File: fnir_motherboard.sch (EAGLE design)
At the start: 44 parts, among them IC1 LTC2494, IC3 AD712R, U2 ATMEGA8U2QFN, X2 USB-SMD-NS, Y1 16MHz

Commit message: new version desinged
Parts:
- added R16: 200, adafruit:R-US_R1206
- added TP1: PTR1B1,27, testpad:PTR1B1,27
- C1, C2, C3, C4, C5, C6, C7, C8: device adafruit:C-USC0805 -> adafruit:C-USC1206
- C10, C9: value (none) -> 0.1uF; device adafruit:C-USC0805 -> adafruit:C-USC1206
- R1: value (none) -> 200; device adafruit:R-US_R0805 -> adafruit:R-US_R1206
- R10, R11, R12, R13, R14, R15, R28, R29, R5, R6, R7, R8, R9: device adafruit:R-US_R0805 -> adafruit:R-US_R1206
- R2: value (none) -> 10k
- R3, R4: value (none) -> 30k; device adafruit:R-US_R0805 -> adafruit:R-US_R1206
- U2: value ATMEGA8U2QFN -> ATMEGA8U2AU; device sparkfun:ATMEGA8U2QFN -> sparkfun:ATMEGA8U2AU
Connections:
- new net N$23: R16.2, SV1.2
- net +5V: now also R2.A; no longer R2.E
- net AGND: now also R2.E; no longer R2.A
- net GND: now also R16.1; no longer SV1.2
- net IR8: now also IC1.CH9; no longer IC1.CH8
- net IR9: now also IC1.CH11; no longer IC1.CH9
- net N$1: now also Q2.G; no longer Q6.G
- net N$12: now also TP1.TP
- net N$2: now also Q1.G; no longer Q7.G
- net N$3: now also Q9.G, U2.PD5; no longer Q5.G, U2.PD4
- net N$4: now also Q4.G; no longer Q1.G
- net N$5: now also Q5.G; no longer Q4.G
- net N$6: now also Q7.G; no longer Q9.G
- net N$7: now also Q6.G; no longer Q2.G
- net N$8: now also U2.PD4; no longer U2.PD5
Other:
- moved on the sheet: C1, C10, C15, C2, C3, C4, C5, C6, C7, C8, C9, IC1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

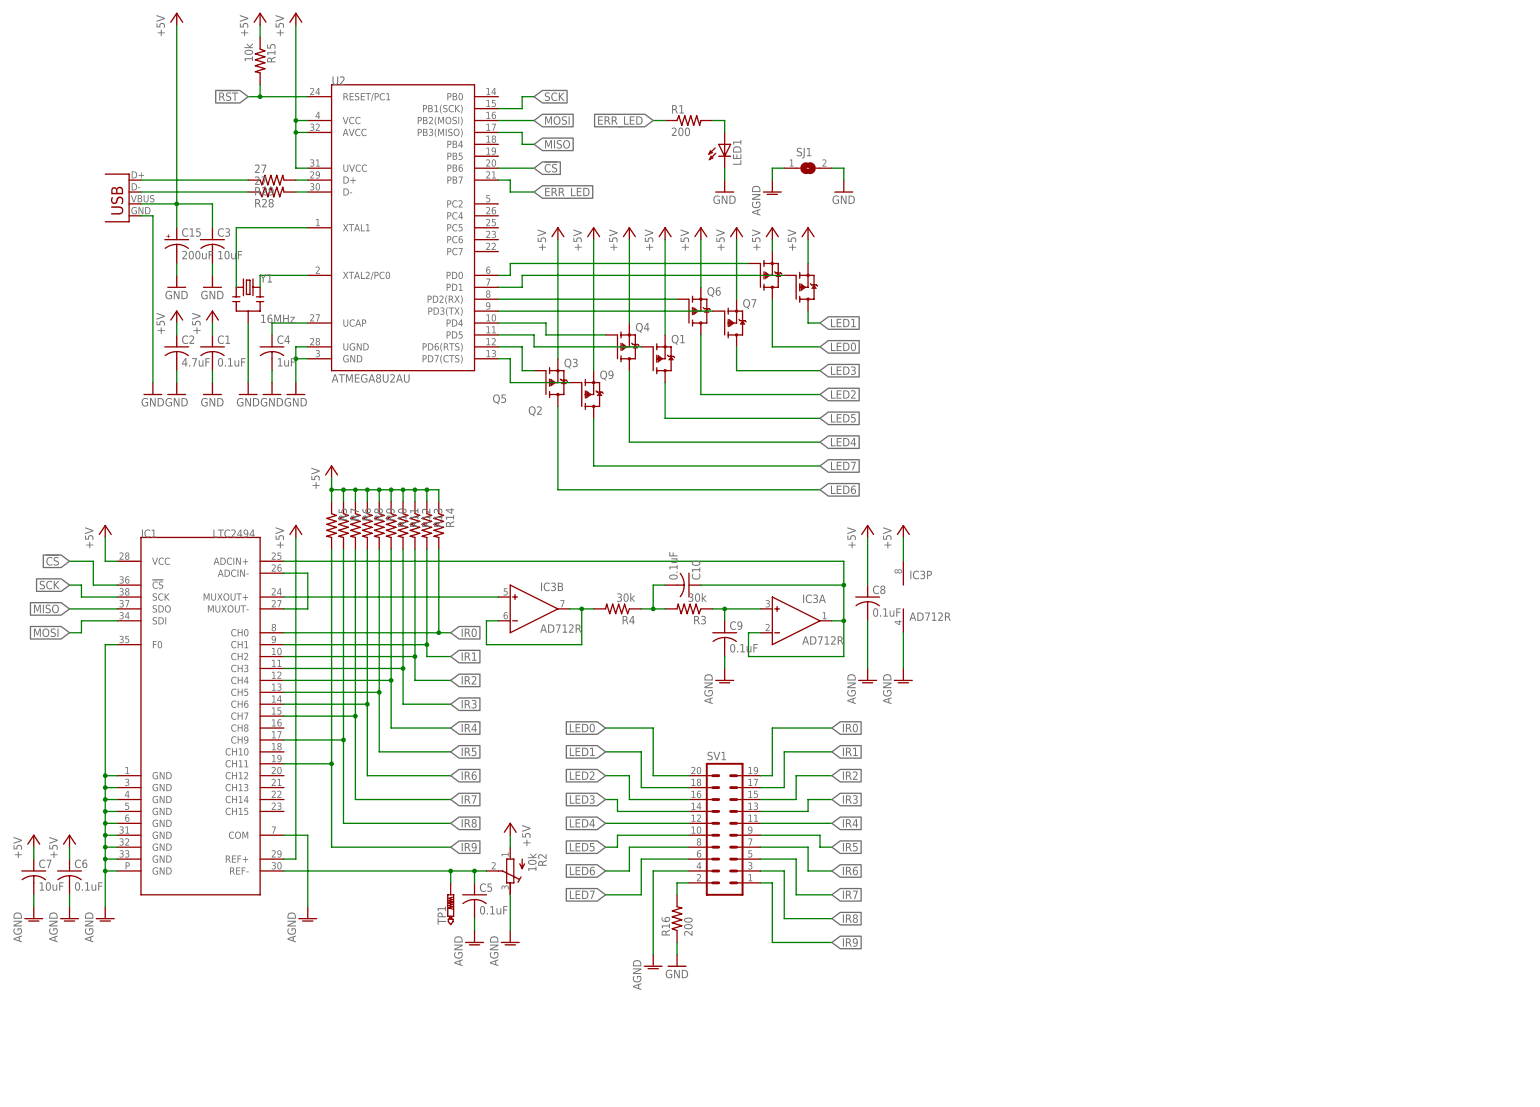
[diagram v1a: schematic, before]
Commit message: slight changes to pour layouts for ground and agnd (merged)
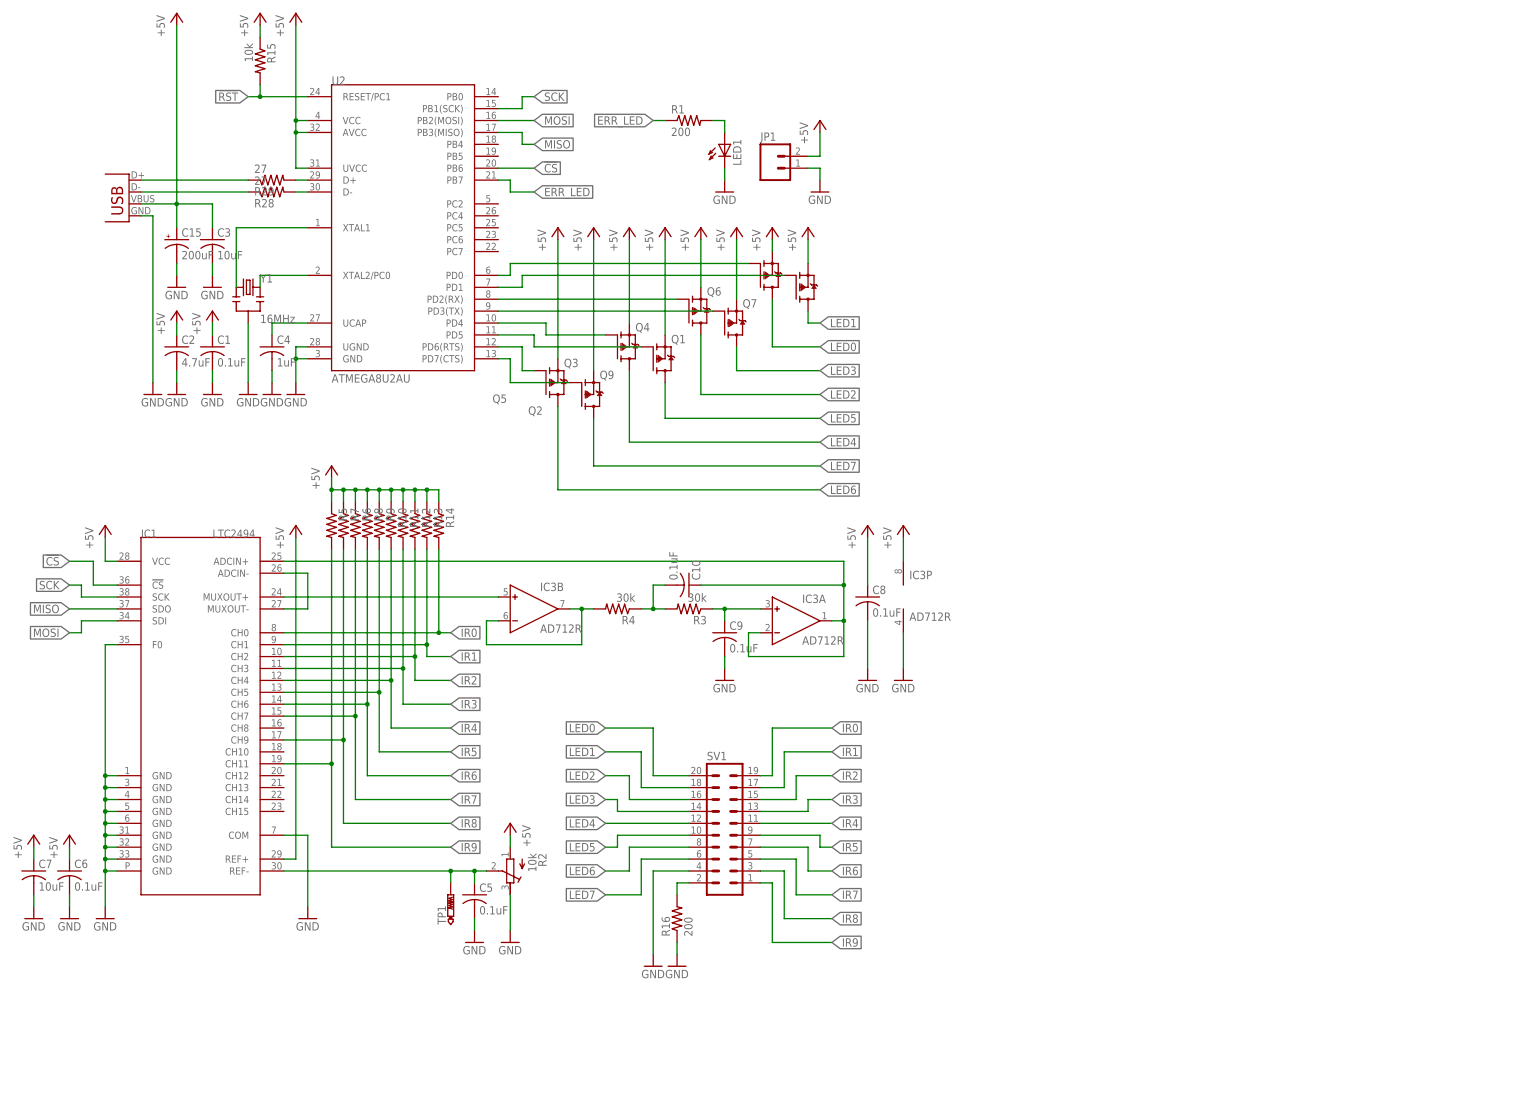
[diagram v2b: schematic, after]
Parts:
- removed SJ1: (no value), jumper:SJ
- added JP1: (no value), sparkfun:M02PTH
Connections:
- removed net AGND: C5.2, C6.2, C7.2, C8.2, C9.2, IC1.COM, IC1.F0, IC1.GND@0, IC1.GND@1, IC1.GND@2, IC1.GND@3, IC1.GND@4, IC1.GND@5, IC1.GND@6, IC1.GND@7, IC1.GND@8, IC3P.V-, R2.E, SJ1.1, SV1.4
- net +5V: now also JP1.2
- net GND: now also C5.2, C6.2, C7.2, C8.2, C9.2, IC1.COM, IC1.F0, IC1.GND@0, IC1.GND@1, IC1.GND@2, IC1.GND@3, IC1.GND@4, IC1.GND@5, IC1.GND@6, IC1.GND@7, IC1.GND@8, IC3P.V-, JP1.1, R2.E, SV1.4; no longer SJ1.2

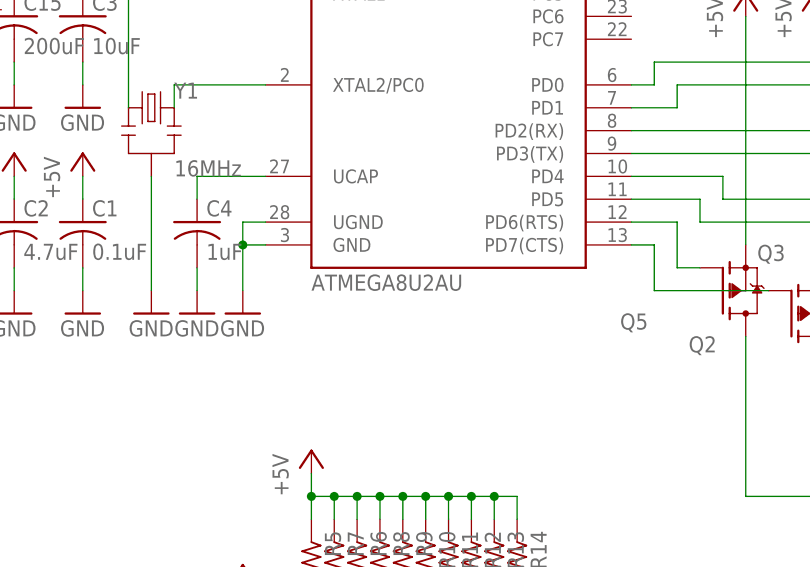
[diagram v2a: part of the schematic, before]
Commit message: updated sch and makefile for 16u2, more space to fit firmware with dfu usb bootloader
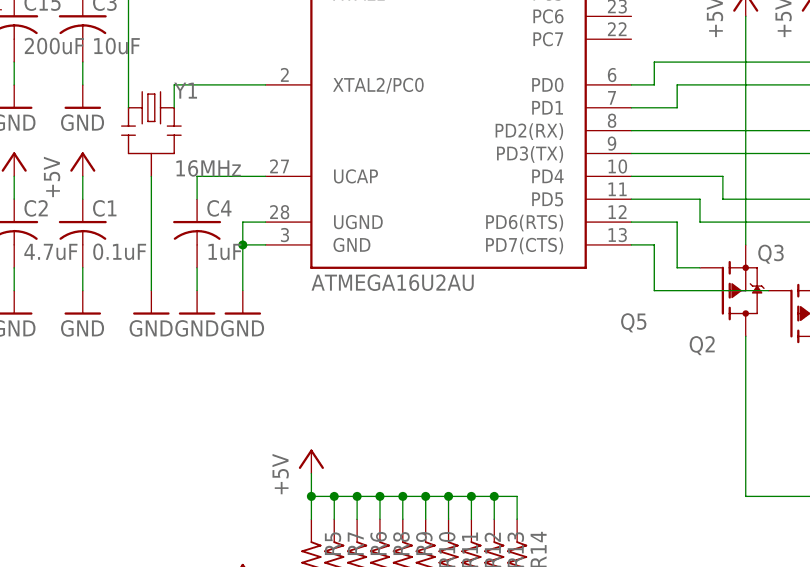
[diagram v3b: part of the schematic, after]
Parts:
- U2: value ATMEGA8U2AU -> ATMEGA16U2AU
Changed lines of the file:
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@@
 <part name="C15" library="adafruit" deviceset="CPOL-US" device="D" value="200uF"/>
 <part name="GND44" library="sparkfun" deviceset="GND" device=""/>
-<part name="U2" library="sparkfun" deviceset="ATMEGA8U2" device="AU"/>
+<part name="U2" library="sparkfun" deviceset="ATMEGA8U2" device="AU" value="ATMEGA16U2AU"/>
 <part name="P+5" library="supply1" deviceset="+5V" device=""/>
 <part name="C4" library="adafruit" deviceset="C-US" device="C1206" value="1uF"/>
